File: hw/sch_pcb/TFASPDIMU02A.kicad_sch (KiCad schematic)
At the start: 34 parts, among them J1 SM04B-GHS-TB, U1 SDP3x, U2 ICM-20948, U3 TCA9617A, U4 MIC5504-3.3YM5-TR, U5 MIC5504-1.8YM5-TR, U6 TCA9617A

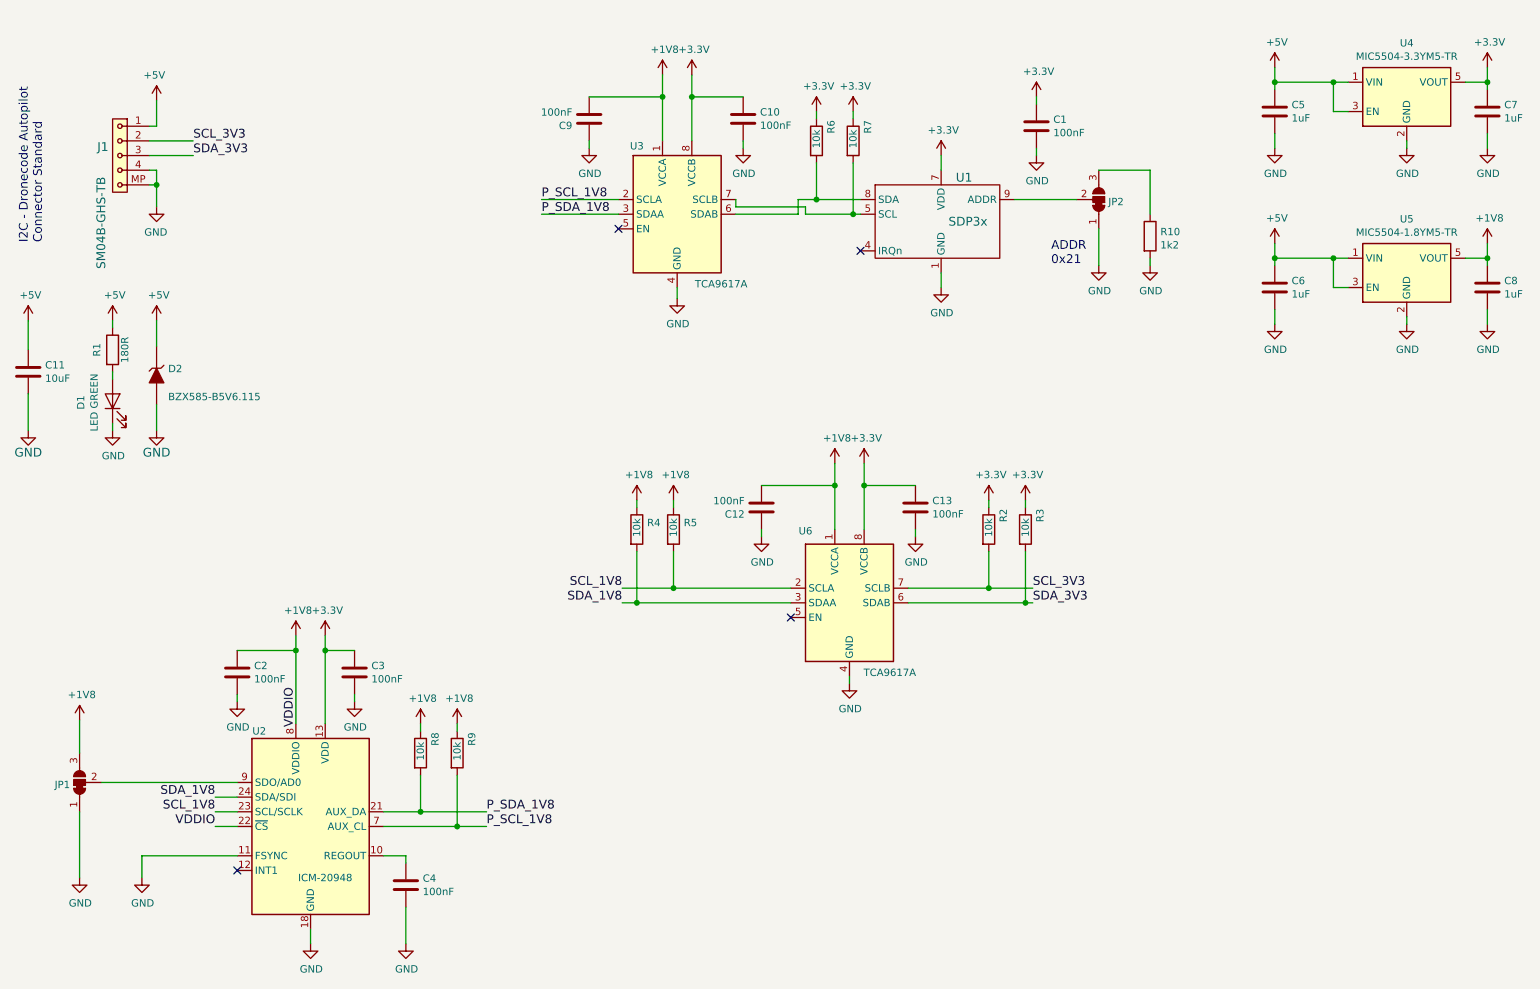
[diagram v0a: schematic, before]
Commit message: Edit schema and PCB
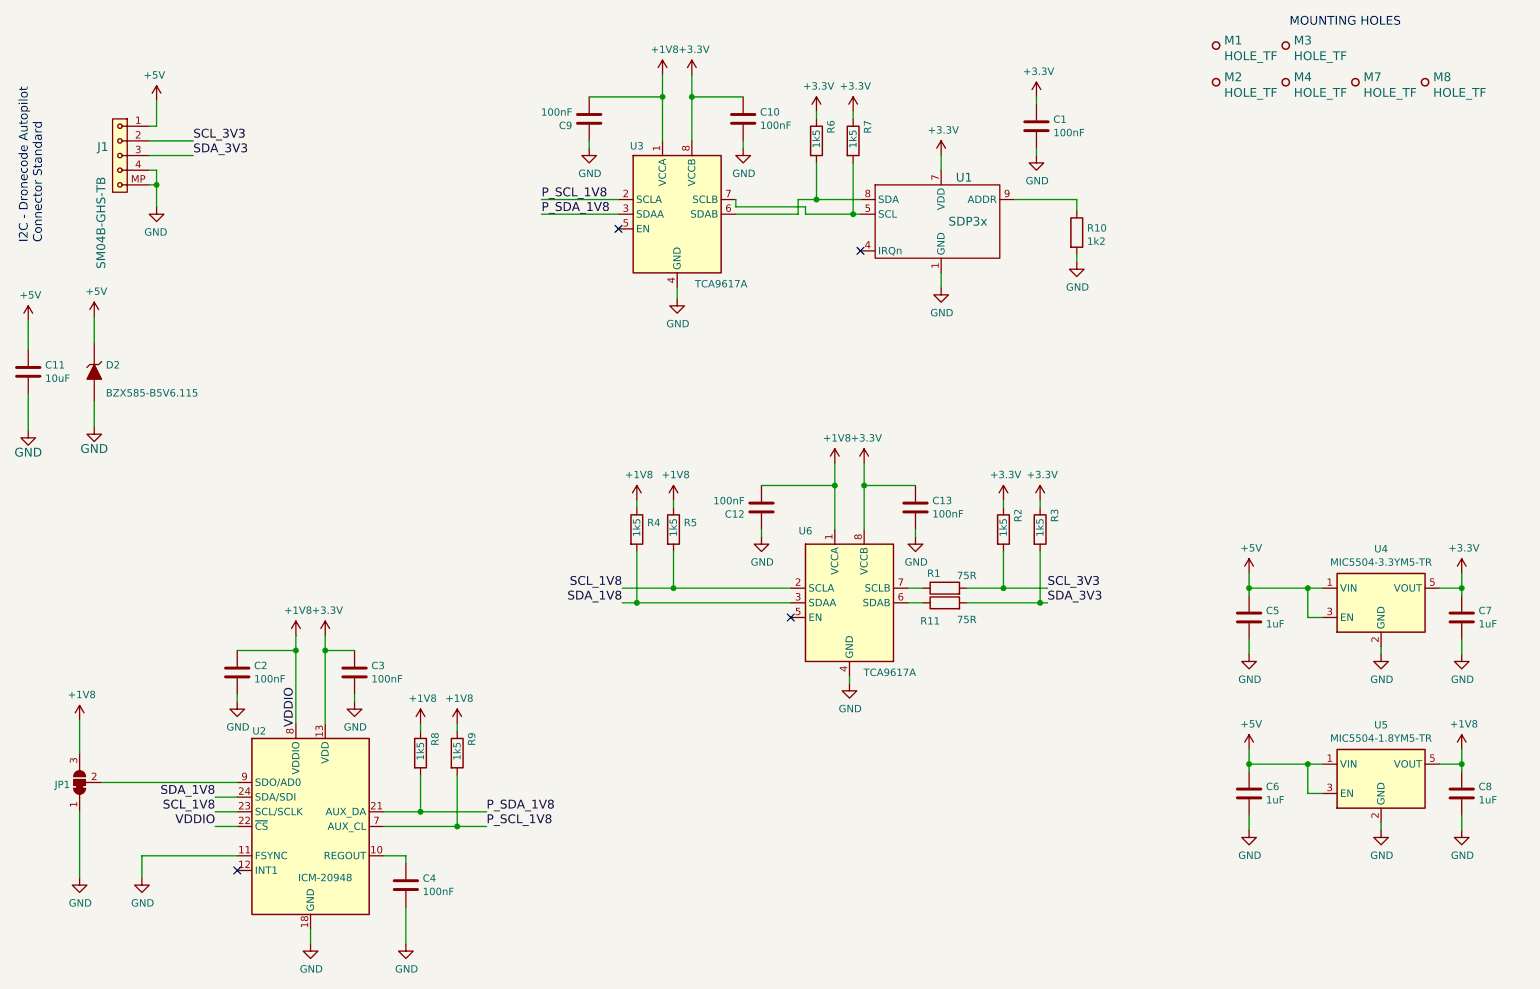
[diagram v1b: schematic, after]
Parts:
- removed D1: LED GREEN, Mlab_D:LED_1206, symbol Device:LED
- removed JP2: SolderJumper_3_Bridged12, symbol Jumper:SolderJumper_3_Bridged12
- added M1, M2, M3, M4, M7, M8: HOLE_TF, Mlab_Mechanical:dira_3mm, symbol MLAB_MECHANICAL:HOLE_TF
- added R11: 75R, Resistor_SMD:R_0402_1005Metric, symbol Device:R
- C1, C10, C12, C13, C2, C3, C4, C5, C6, C7, C8, C9: footprint Mlab_R:SMD-0603 -> Capacitor_SMD:C_0402_1005Metric
- C11: footprint Mlab_R:SMD-0805 -> Capacitor_SMD:C_0402_1005Metric
- JP1: footprint (none) -> Jumper:SolderJumper-3_P1.3mm_Bridged12_RoundedPad1.0x1.5mm
- R1: value 180R -> 75R; footprint Mlab_R:SMD-0603 -> Resistor_SMD:R_0402_1005Metric; UST_ID 5c70984512875079b91f8957 -> (none)
- R10: footprint (none) -> Resistor_SMD:R_0402_1005Metric
- R2, R3, R4, R5, R6, R7, R8, R9: value 10k -> 1k5; footprint Mlab_R:SMD-0603 -> Resistor_SMD:R_0402_1005Metric; UST_ID 5c70984612875079b91f899f -> (none)
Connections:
- net +5V: no longer R1.1
- net SCL_3V3: now also R1.2; no longer U6.7 (SCLB)
- net SDA_3V3: now also R11.2; no longer U6.6 (SDAB)
- net at U1.9 (ADDR): now also R10.1
- new net: R11.1, U6.6 (SDAB)
- new net: R1.1, U6.7 (SCLB)
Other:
- note added: "MOUNTING HOLES"
- note removed: "ADDR 0x21"
- moved on the sheet: C5, C6, C7, C8, D2, R10, R2, R3, U4, U5

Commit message: Edit PCB
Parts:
- added JP2: SolderJumper_3_Bridged12, Jumper:SolderJumper-3_P1.3mm_Bridged12_RoundedPad1.0x1.5mm, symbol Jumper:SolderJumper_3_Bridged12
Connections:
- net GND: now also JP2.1 (A)
- net at U1.9 (ADDR): now also JP2.2 (C); no longer R10.1
- new net: JP2.3 (B), R10.1
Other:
- moved on the sheet: R10
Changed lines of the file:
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@@
     (stroke (width 0) (type solid) (color 0 0 0 0))
   )
-  (wire (pts (xy 204.47 45.72) (xy 204.47 47.625))
-    (stroke (width 0) (type solid) (color 0 0 0 0))
-  )
-  (wire (pts (xy 204.47 55.245) (xy 204.47 56.515))
+  (wire (pts (xy 208.28 40.005) (xy 217.17 40.005))
+    (stroke (width 0) (type solid) (color 0 0 0 0))
+  )
+  (wire (pts (xy 208.28 40.64) (xy 208.28 40.005))
+    (stroke (width 0) (type solid) (color 0 0 0 0))
+  )
+  (wire (pts (xy 208.28 50.8) (xy 208.28 60.96))
+    (stroke (width 0) (type solid) (color 0 0 0 0))
+  )
+  (wire (pts (xy 217.17 40.005) (xy 217.17 52.07))
+    (stroke (width 0) (type solid) (color 0 0 0 0))
+  )
+  (wire (pts (xy 217.17 59.69) (xy 217.17 60.96))
     (stroke (width 0) (type solid) (color 0 0 0 0))
   )
@@
     (pin "1")
   )
-  (symbol (lib_id "power:GND") (at 204.47 56.515 0) (unit 1)
-    (in_bom yes) (on_board yes)
-    (property "Reference" "#PWR014" (id 0) (at 204.47 62.865 0)
-      (effects (font (size 1.27 1.27)) hide)
-    )
-    (property "Value" "GND" (id 1) (at 204.597 60.9092 0))
-    (property "Footprint" "" (id 2) (at 204.47 56.515 0)
-      (effects (font (size 1.27 1.27)) hide)
-    )
-    (property "Datasheet" "" (id 3) (at 204.47 56.515 0)
+  (symbol (lib_id "power:GND") (at 208.28 60.96 0) (unit 1)
+    (in_bom yes) (on_board yes)
+    (property "Reference" "#PWR0102" (id 0) (at 208.28 67.31 0)
+      (effects (font (size 1.27 1.27)) hide)
+    )
+    (property "Value" "GND" (id 1) (at 208.407 65.3542 0))
+    (property "Footprint" "" (id 2) (at 208.28 60.96 0)
+      (effects (font (size 1.27 1.27)) hide)
+    )
+    (property "Datasheet" "" (id 3) (at 208.28 60.96 0)
+      (effects (font (size 1.27 1.27)) hide)
+    )
+    (pin "1")
+  )
+  (symbol (lib_id "power:GND") (at 217.17 60.96 0) (unit 1)
+    (in_bom yes) (on_board yes)
+    (property "Reference" "#PWR014" (id 0) (at 217.17 67.31 0)
+      (effects (font (size 1.27 1.27)) hide)
+    )
+    (property "Value" "GND" (id 1) (at 217.297 65.3542 0))
+    (property "Footprint" "" (id 2) (at 217.17 60.96 0)
+      (effects (font (size 1.27 1.27)) hide)
+    )
+    (property "Datasheet" "" (id 3) (at 217.17 60.96 0)
       (effects (font (size 1.27 1.27)) hide)
     )
@@
     (pin "2")
   )
-  (symbol (lib_id "Device:R") (at 204.47 51.435 0) (unit 1)
+  (symbol (lib_id "Device:R") (at 217.17 55.88 0) (unit 1)
     (in_bom yes) (on_board yes) (fields_autoplaced)
-    (property "Reference" "R10" (id 0) (at 206.2481 50.6741 0)
-      (effects (font (size 1.27 1.27)) (justify left))
-    )
-    (property "Value" "1k2" (id 1) (at 206.2481 52.9728 0)
-      (effects (font (size 1.27 1.27)) (justify left))
-    )
-    (property "Footprint" "Resistor_SMD:R_0402_1005Metric" (id 2) (at 202.692 51.435 90)
-      (effects (font (size 1.27 1.27)) hide)
-    )
-    (property "Datasheet" "~" (id 3) (at 204.47 51.435 0)
+    (property "Reference" "R10" (id 0) (at 218.9481 55.1191 0)
+      (effects (font (size 1.27 1.27)) (justify left))
+    )
+    (property "Value" "1k2" (id 1) (at 218.9481 57.4178 0)
+      (effects (font (size 1.27 1.27)) (justify left))
+    )
+    (property "Footprint" "Resistor_SMD:R_0402_1005Metric" (id 2) (at 215.392 55.88 90)
+      (effects (font (size 1.27 1.27)) hide)
+    )
+    (property "Datasheet" "~" (id 3) (at 217.17 55.88 0)
       (effects (font (size 1.27 1.27)) hide)
     )
@@
     )
     (property "Datasheet" "~" (id 3) (at 31.75 146.685 0)
+      (effects (font (size 1.27 1.27)) hide)
+    )
+    (pin "1")
+    (pin "2")
+    (pin "3")
+  )
+  (symbol (lib_id "Jumper:SolderJumper_3_Bridged12") (at 208.28 45.72 270) (mirror x) (unit 1)
+    (in_bom yes) (on_board yes) (fields_autoplaced)
+    (property "Reference" "JP2" (id 0) (at 209.9311 46.1085 90)
+      (effects (font (size 1.27 1.27)) (justify left))
+    )
+    (property "Value" "SolderJumper_3_Bridged12" (id 1) (at 209.931 47.2578 90)
+      (effects (font (size 1.27 1.27)) (justify left) hide)
+    )
+    (property "Footprint" "Jumper:SolderJumper-3_P1.3mm_Bridged12_RoundedPad1.0x1.5mm" (id 2) (at 208.28 45.72 0)
+      (effects (font (size 1.27 1.27)) hide)
+    )
+    (property "Datasheet" "~" (id 3) (at 208.28 45.72 0)
       (effects (font (size 1.27 1.27)) hide)
     )
@@
       (reference "#PWR0101") (unit 1) (value "GND") (footprint "")
     )
+    (path "/8e51e99e-a8a4-46ab-bb52-01ad4336ba73"
+      (reference "#PWR0102") (unit 1) (value "GND") (footprint "")
+    )
     (path "/00000000-0000-0000-0000-00005c6383c2"
       (reference "#PWR0103") (unit 1) (value "+3.3V") (footprint "")
@@
       (reference "JP1") (unit 1) (value "SolderJumper_3_Bridged12") (footprint "Jumper:SolderJumper-3_P1.3mm_Bridged12_RoundedPad1.0x1.5mm")
     )
+    (path "/80d8341b-0790-4d4a-93eb-0881540aa859"
+      (reference "JP2") (unit 1) (value "SolderJumper_3_Bridged12") (footprint "Jumper:SolderJumper-3_P1.3mm_Bridged12_RoundedPad1.0x1.5mm")
+    )
     (path "/fc79bf5f-0ecf-4cae-a035-120c2c327676"

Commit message: Edit PCB. #1
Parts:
- removed M4, M8: HOLE_TF, Mlab_Mechanical:dira_3mm, symbol MLAB_MECHANICAL:HOLE_TF
- R10: value 1k2 -> 2k7
- R2, R3: value 1k5 -> 2k7
- R4, R5, R6, R7, R8, R9: value 1k5 -> 10k
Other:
- moved on the sheet: M2, M3, M7
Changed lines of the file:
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@@
-(kicad_sch (version 20210621) (generator eeschema)
+(kicad_sch (version 20210406) (generator eeschema)
   (paper "A4")
   (title_block
@@
     )
   )
-  (symbol (lib_id "MLAB_MECHANICAL:HOLE_TF") (at 228.6 25.4 0) (unit 1)
+  (symbol (lib_id "MLAB_MECHANICAL:HOLE_TF") (at 241.3 19.05 0) (unit 1)
     (in_bom yes) (on_board yes) (fields_autoplaced)
-    (property "Reference" "M2" (id 0) (at 229.9971 24.5124 0)
+    (property "Reference" "M2" (id 0) (at 242.6971 18.1624 0)
       (effects (font (size 1.524 1.524)) (justify left))
     )
-    (property "Value" "HOLE_TF" (id 1) (at 229.9971 27.22 0)
+    (property "Value" "HOLE_TF" (id 1) (at 242.6971 20.87 0)
       (effects (font (size 1.524 1.524)) (justify left))
     )
-    (property "Footprint" "Mlab_Mechanical:dira_3mm" (id 2) (at 228.6 25.4 0)
+    (property "Footprint" "Mlab_Mechanical:dira_3mm" (id 2) (at 241.3 19.05 0)
       (effects (font (size 1.524 1.524)) hide)
     )
-    (property "Datasheet" "" (id 3) (at 228.6 25.4 0)
+    (property "Datasheet" "" (id 3) (at 241.3 19.05 0)
       (effects (font (size 1.524 1.524)))
     )
   )
-  (symbol (lib_id "MLAB_MECHANICAL:HOLE_TF") (at 240.665 19.05 0) (unit 1)
+  (symbol (lib_id "MLAB_MECHANICAL:HOLE_TF") (at 254 19.05 0) (unit 1)
     (in_bom yes) (on_board yes) (fields_autoplaced)
-    (property "Reference" "M3" (id 0) (at 242.0621 18.1624 0)
+    (property "Reference" "M3" (id 0) (at 255.3971 18.1624 0)
       (effects (font (size 1.524 1.524)) (justify left))
     )
-    (property "Value" "HOLE_TF" (id 1) (at 242.0621 20.87 0)
+    (property "Value" "HOLE_TF" (id 1) (at 255.3971 20.87 0)
       (effects (font (size 1.524 1.524)) (justify left))
     )
-    (property "Footprint" "Mlab_Mechanical:dira_3mm" (id 2) (at 240.665 19.05 0)
+    (property "Footprint" "Mlab_Mechanical:dira_3mm" (id 2) (at 254 19.05 0)
       (effects (font (size 1.524 1.524)) hide)
     )
-    (property "Datasheet" "" (id 3) (at 240.665 19.05 0)
+    (property "Datasheet" "" (id 3) (at 254 19.05 0)
       (effects (font (size 1.524 1.524)))
     )
   )
-  (symbol (lib_id "MLAB_MECHANICAL:HOLE_TF") (at 240.665 25.4 0) (unit 1)
+  (symbol (lib_id "MLAB_MECHANICAL:HOLE_TF") (at 266.065 19.05 0) (unit 1)
     (in_bom yes) (on_board yes) (fields_autoplaced)
-    (property "Reference" "M4" (id 0) (at 242.0621 24.5124 0)
+    (property "Reference" "M7" (id 0) (at 267.4621 18.1624 0)
       (effects (font (size 1.524 1.524)) (justify left))
     )
-    (property "Value" "HOLE_TF" (id 1) (at 242.0621 27.22 0)
+    (property "Value" "HOLE_TF" (id 1) (at 267.4621 20.87 0)
       (effects (font (size 1.524 1.524)) (justify left))
     )
-    (property "Footprint" "Mlab_Mechanical:dira_3mm" (id 2) (at 240.665 25.4 0)
+    (property "Footprint" "Mlab_Mechanical:dira_3mm" (id 2) (at 266.065 19.05 0)
       (effects (font (size 1.524 1.524)) hide)
     )
-    (property "Datasheet" "" (id 3) (at 240.665 25.4 0)
-      (effects (font (size 1.524 1.524)))
-    )
-  )
-  (symbol (lib_id "MLAB_MECHANICAL:HOLE_TF") (at 252.73 25.4 0) (unit 1)
-    (in_bom yes) (on_board yes) (fields_autoplaced)
-    (property "Reference" "M7" (id 0) (at 254.1271 24.5124 0)
-      (effects (font (size 1.524 1.524)) (justify left))
-    )
-    (property "Value" "HOLE_TF" (id 1) (at 254.1271 27.22 0)
-      (effects (font (size 1.524 1.524)) (justify left))
-    )
-    (property "Footprint" "Mlab_Mechanical:dira_3mm" (id 2) (at 252.73 25.4 0)
-      (effects (font (size 1.524 1.524)) hide)
-    )
-    (property "Datasheet" "" (id 3) (at 252.73 25.4 0)
-      (effects (font (size 1.524 1.524)))
-    )
-  )
-  (symbol (lib_id "MLAB_MECHANICAL:HOLE_TF") (at 264.795 25.4 0) (unit 1)
-    (in_bom yes) (on_board yes) (fields_autoplaced)
-    (property "Reference" "M8" (id 0) (at 266.1921 24.5124 0)
-      (effects (font (size 1.524 1.524)) (justify left))
-    )
-    (property "Value" "HOLE_TF" (id 1) (at 266.1921 27.22 0)
-      (effects (font (size 1.524 1.524)) (justify left))
-    )
-    (property "Footprint" "Mlab_Mechanical:dira_3mm" (id 2) (at 264.795 25.4 0)
-      (effects (font (size 1.524 1.524)) hide)
-    )
-    (property "Datasheet" "" (id 3) (at 264.795 25.4 0)
+    (property "Datasheet" "" (id 3) (at 266.065 19.05 0)
       (effects (font (size 1.524 1.524)))
     )
@@
       (effects (font (size 1.27 1.27)) (justify left))
     )
-    (property "Value" "1k5" (id 1) (at 90.805 142.875 90)
+    (property "Value" "10k" (id 1) (at 90.805 142.875 90)
       (effects (font (size 1.27 1.27)) (justify left))
     )
@@
       (effects (font (size 1.27 1.27)) (justify left))
     )
-    (property "Value" "1k5" (id 1) (at 97.155 142.875 90)
+    (property "Value" "10k" (id 1) (at 97.155 142.875 90)
       (effects (font (size 1.27 1.27)) (justify left))
     )
@@
       (effects (font (size 1.27 1.27)) (justify left))
     )
-    (property "Value" "1k5" (id 1) (at 128.27 104.14 90)
+    (property "Value" "10k" (id 1) (at 128.27 104.14 90)
       (effects (font (size 1.27 1.27)) (justify left))
     )
@@
       (effects (font (size 1.27 1.27)) (justify left))
     )
-    (property "Value" "1k5" (id 1) (at 134.62 104.14 90)
+    (property "Value" "10k" (id 1) (at 134.62 104.14 90)
       (effects (font (size 1.27 1.27)) (justify left))
     )
@@
       (effects (font (size 1.27 1.27)) (justify left))
     )
-    (property "Value" "1k5" (id 1) (at 159.385 36.83 90)
+    (property "Value" "10k" (id 1) (at 159.385 36.83 90)
       (effects (font (size 1.27 1.27)) (justify left))
     )
@@
       (effects (font (size 1.27 1.27)) (justify left))
     )
-    (property "Value" "1k5" (id 1) (at 165.735 36.83 90)
+    (property "Value" "10k" (id 1) (at 165.735 36.83 90)
       (effects (font (size 1.27 1.27)) (justify left))
     )
@@
       (effects (font (size 1.27 1.27)) (justify left))
     )
-    (property "Value" "1k5" (id 1) (at 191.77 104.14 90)
+    (property "Value" "2k7" (id 1) (at 191.77 104.14 90)
       (effects (font (size 1.27 1.27)) (justify left))
     )
@@
       (effects (font (size 1.27 1.27)) (justify left))
     )
-    (property "Value" "1k5" (id 1) (at 198.12 104.14 90)
+    (property "Value" "2k7" (id 1) (at 198.12 104.14 90)
       (effects (font (size 1.27 1.27)) (justify left))
     )
@@
       (effects (font (size 1.27 1.27)) (justify left))
     )
-    (property "Value" "1k2" (id 1) (at 218.9481 57.4178 0)
+    (property "Value" "2k7" (id 1) (at 218.9481 57.4178 0)
       (effects (font (size 1.27 1.27)) (justify left))
     )
@@
       (reference "M3") (unit 1) (value "HOLE_TF") (footprint "Mlab_Mechanical:dira_3mm")
     )
-    (path "/13e6ce0e-70eb-42f0-a33f-43e3ea889023"
-      (reference "M4") (unit 1) (value "HOLE_TF") (footprint "Mlab_Mechanical:dira_3mm")
-    )
     (path "/93267269-2845-42f9-ad7b-3734adaa240a"
       (reference "M7") (unit 1) (value "HOLE_TF") (footprint "Mlab_Mechanical:dira_3mm")
     )
-    (path "/fa96f8b2-4d27-4287-b50d-5a42a24fa3c6"
-      (reference "M8") (unit 1) (value "HOLE_TF") (footprint "Mlab_Mechanical:dira_3mm")
-    )
     (path "/e4dfbc85-d0dd-4f57-aec3-6bf8216c0a9c"
       (reference "R1") (unit 1) (value "75R") (footprint "Resistor_SMD:R_0402_1005Metric")
     )
     (path "/030b68df-bcf5-4e1a-ae05-d7222742ea2b"
-      (reference "R2") (unit 1) (value "1k5") (footprint "Resistor_SMD:R_0402_1005Metric")
+      (reference "R2") (unit 1) (value "2k7") (footprint "Resistor_SMD:R_0402_1005Metric")
     )
     (path "/dc183c1a-cb80-49ed-94bf-009469c44d7e"
-      (reference "R3") (unit 1) (value "1k5") (footprint "Resistor_SMD:R_0402_1005Metric")
+      (reference "R3") (unit 1) (value "2k7") (footprint "Resistor_SMD:R_0402_1005Metric")
     )
     (path "/00000000-0000-0000-0000-00005c6e3c9a"
-      (reference "R4") (unit 1) (value "1k5") (footprint "Resistor_SMD:R_0402_1005Metric")
+      (reference "R4") (unit 1) (value "10k") (footprint "Resistor_SMD:R_0402_1005Metric")
     )
     (path "/00000000-0000-0000-0000-00005c6e3eeb"
-      (reference "R5") (unit 1) (value "1k5") (footprint "Resistor_SMD:R_0402_1005Metric")
+      (reference "R5") (unit 1) (value "10k") (footprint "Resistor_SMD:R_0402_1005Metric")
     )
     (path "/00000000-0000-0000-0000-00005c6bdd86"
-      (reference "R6") (unit 1) (value "1k5") (footprint "Resistor_SMD:R_0402_1005Metric")
+      (reference "R6") (unit 1) (value "10k") (footprint "Resistor_SMD:R_0402_1005Metric")
     )
     (path "/00000000-0000-0000-0000-00005c6be380"
-      (reference "R7") (unit 1) (value "1k5") (footprint "Resistor_SMD:R_0402_1005Metric")
+      (reference "R7") (unit 1) (value "10k") (footprint "Resistor_SMD:R_0402_1005Metric")
     )
     (path "/00000000-0000-0000-0000-00005c6ca62c"
-      (reference "R8") (unit 1) (value "1k5") (footprint "Resistor_SMD:R_0402_1005Metric")
+      (reference "R8") (unit 1) (value "10k") (footprint "Resistor_SMD:R_0402_1005Metric")
     )
     (path "/00000000-0000-0000-0000-00005c6cbd6b"
-      (reference "R9") (unit 1) (value "1k5") (footprint "Resistor_SMD:R_0402_1005Metric")
+      (reference "R9") (unit 1) (value "10k") (footprint "Resistor_SMD:R_0402_1005Metric")
     )
     (path "/3aa428a0-ceb5-4f74-91bf-8a6aa9655738"
-      (reference "R10") (unit 1) (value "1k2") (footprint "Resistor_SMD:R_0402_1005Metric")
+      (reference "R10") (unit 1) (value "2k7") (footprint "Resistor_SMD:R_0402_1005Metric")
     )
     (path "/0832c9ae-234f-441f-8ba2-ada66ecf3422"
